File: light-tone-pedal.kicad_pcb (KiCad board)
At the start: 2 copper layers, 73.2 x 97.5 mm, 56 parts, among them U1 LM358AP, U2 LM358AP, U3 LM358AP

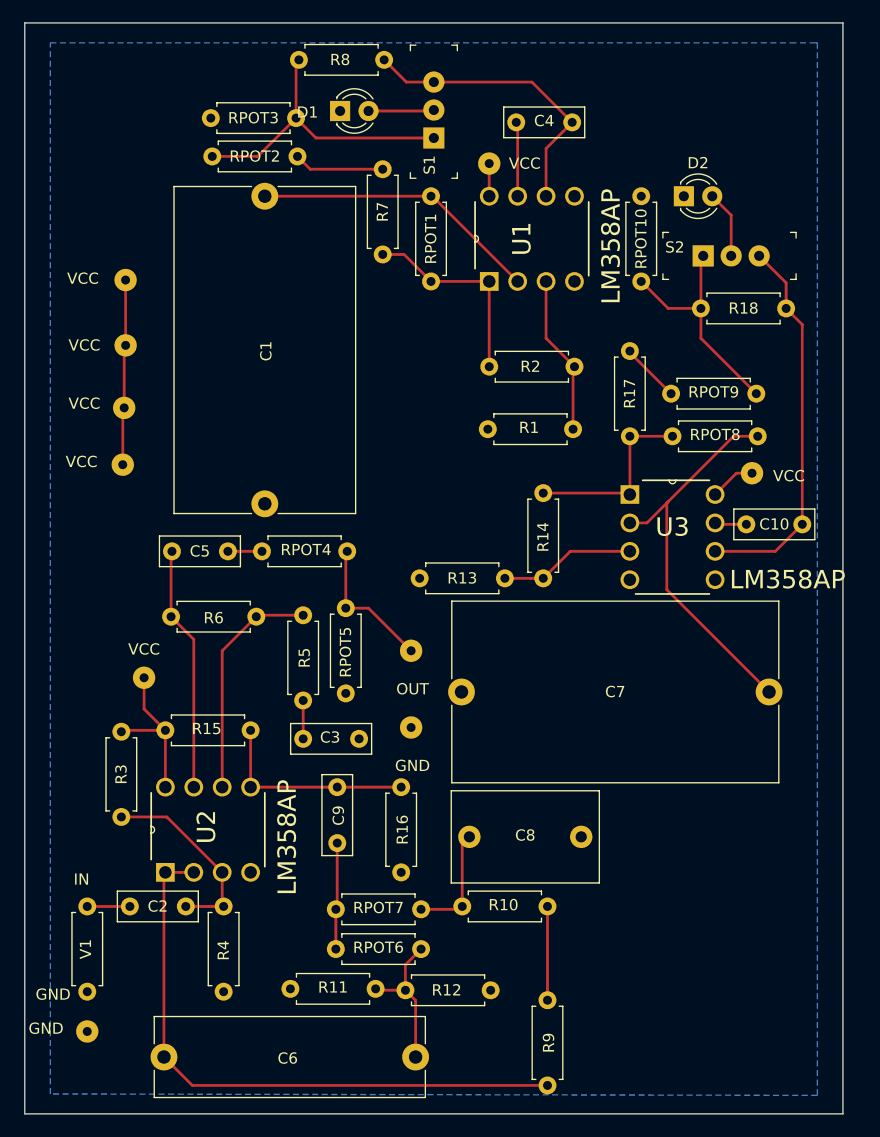
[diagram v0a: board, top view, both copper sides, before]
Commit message: Updated pdf of circuit schematic. Made pcb for light affected tone pedal.
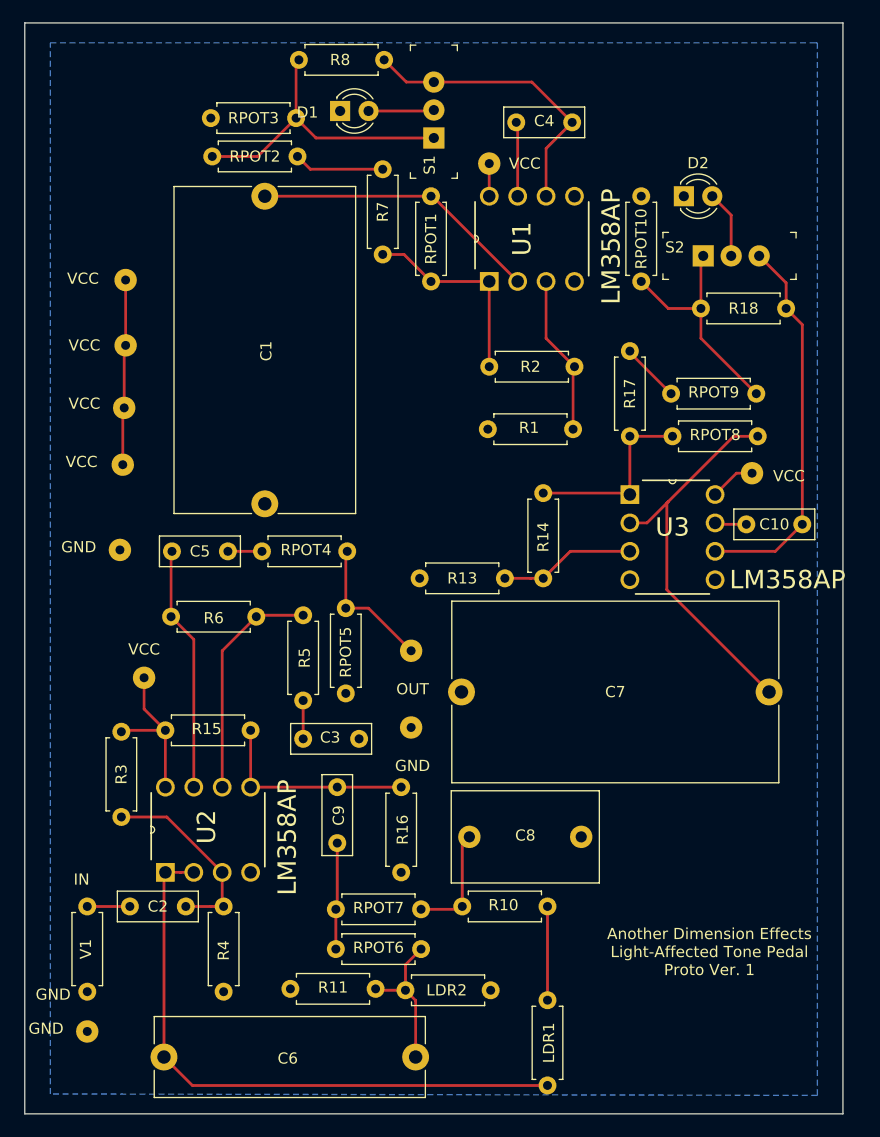
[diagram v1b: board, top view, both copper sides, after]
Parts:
- added GND: SolderWirePad_1x01_Drill0.8mm, Connector_Wire:SolderWirePad_1x01_Drill0.8mm, F.Cu at (102.7, 83.4)
- LDR1: renamed from R9; value 3k -> RLDR3k-11k
- LDR2: renamed from R12; value 3k -> RLDR3k-11k
- RPOT1, RPOT8: value R -> R20kLin
- RPOT10, RPOT2, RPOT3, RPOT9: value R -> R10kLin
- RPOT4, RPOT5: value R -> R1MegLog
- RPOT6, RPOT7: value R -> R100kLin
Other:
- board text added: "Another Dimension Effects Light-Affected Tone Pedal Proto Ver. 1"

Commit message: Added a low pass filter to power of circuit to take out noise from power supply.
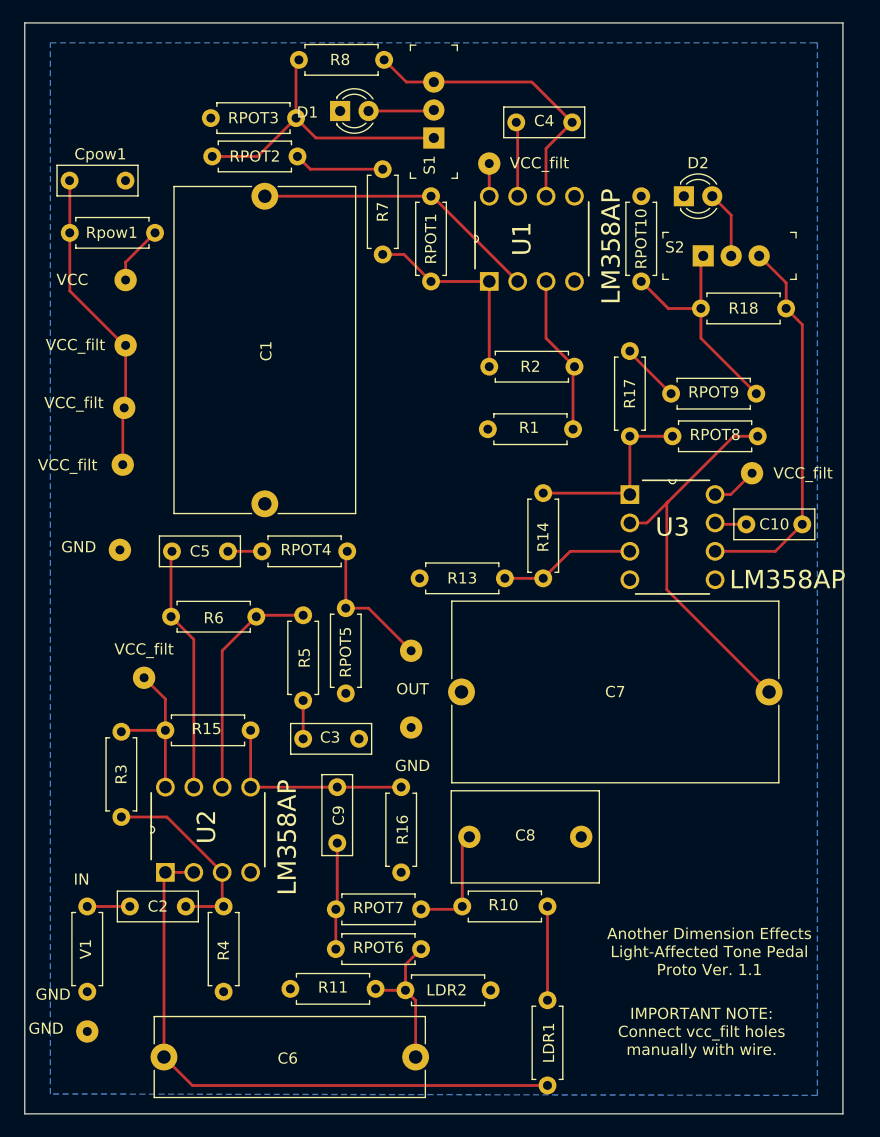
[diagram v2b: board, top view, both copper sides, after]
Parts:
- removed the VCC at (103.0, 75.8)
- removed the VCC at (103.1, 70.7)
- removed the VCC at (103.3, 65.2)
- added Cpow1: 100u, Capacitor_THT:C_Disc_D7.0mm_W2.5mm_P5.00mm, F.Cu at (98.2, 50.4)
- added Rpow1: 200, Resistor_THT:R_Axial_DIN0207_L6.3mm_D2.5mm_P7.62mm_Horizontal, F.Cu at (98.3, 55.1)
- added VCC_filt: SolderWirePad_1x01_Drill0.8mm, Connector_Wire:SolderWirePad_1x01_Drill0.8mm, F.Cu at (103.0, 75.8)
- added VCC_filt: SolderWirePad_1x01_Drill0.8mm, Connector_Wire:SolderWirePad_1x01_Drill0.8mm, F.Cu at (103.1, 70.7)
- added VCC_filt: SolderWirePad_1x01_Drill0.8mm, Connector_Wire:SolderWirePad_1x01_Drill0.8mm, F.Cu at (103.3, 65.2)
- renumbered VCC to VCC_filt
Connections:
- R15 pad 1: VCC -> vcc_filtered
- R3 pad 1: VCC -> vcc_filtered
- U1 pad 8: VCC -> vcc_filtered
- U2 pad 8: VCC -> vcc_filtered
- U3 pad 8: VCC -> vcc_filtered
- VCC_filt pad 1: VCC -> vcc_filtered (x3)
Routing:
- net vcc_filtered: track 0.00 -> 49.4 mm
- net VCC: track 38.2 -> 5.31 mm
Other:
- board text added: "Another Dimension Effects Light-Affected Tone Pedal Proto Ver. 1.1"
- board text added: "IMPORTANT NOTE: Connect vcc_filt holes manually with wire."
- board text removed: "Another Dimension Effects Light-Affected Tone Pedal Proto Ver. 1"

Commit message: Added polarity symbols on pcb for capacitors for the case of when polarized capacitors are used.
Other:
- board text added: "+"
- board text added: "-"
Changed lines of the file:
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@@
   (general
     (thickness 1.6)
-    (drawings 8)
+    (drawings 30)
     (tracks 127)
     (zones 0)
@@
     (visible_elements FFFFFF7F)
     (pcbplotparams
-      (layerselection 0x3d0fc_ffffffff)
+      (layerselection 0x3d0ff_ffffffff)
       (usegerberextensions false)
       (usegerberattributes false)
@@
     )
   )
+  (gr_text + (at 119.08028 102.44582) (layer F.SilkS)
+    (effects (font (size 1 1) (thickness 0.15)))
+  )
+  (gr_text - (at 124.079 102.53726) (layer F.SilkS)
+    (effects (font (size 1 1) (thickness 0.15)))
+  )
+  (gr_text - (at 112.52708 85.93074) (layer F.SilkS)
+    (effects (font (size 1 1) (thickness 0.15)))
+  )
+  (gr_text + (at 107.25912 85.88502) (layer F.SilkS)
+    (effects (font (size 1 1) (thickness 0.15)))
+  )
+  (gr_text - (at 108.68152 117.51056) (layer F.SilkS)
+    (effects (font (size 1 1) (thickness 0.15)))
+  )
+  (gr_text + (at 103.36784 117.57406) (layer F.SilkS)
+    (effects (font (size 1 1) (thickness 0.15)))
+  )
+  (gr_text + (at 97.45472 48.22952) (layer F.SilkS)
+    (effects (font (size 1 1) (thickness 0.15)))
+  )
+  (gr_text - (at 104.21366 48.42256) (layer F.SilkS)
+    (effects (font (size 1 1) (thickness 0.15)))
+  )
+  (gr_text + (at 109.31398 128.78054) (layer F.SilkS)
+    (effects (font (size 1 1) (thickness 0.15)))
+  )
+  (gr_text - (at 126.52502 128.53416) (layer F.SilkS)
+    (effects (font (size 1 1) (thickness 0.15)))
+  )
+  (gr_text - (at 143.90116 106.3625) (layer F.SilkS)
+    (effects (font (size 1 1) (thickness 0.15)))
+  )
+  (gr_text + (at 133.94182 106.20756) (layer F.SilkS)
+    (effects (font (size 1 1) (thickness 0.15)))
+  )
+  (gr_text + (at 157.90672 95.9739) (layer F.SilkS)
+    (effects (font (size 1 1) (thickness 0.15)))
+  )
+  (gr_text - (at 136.68502 95.9739) (layer F.SilkS)
+    (effects (font (size 1 1) (thickness 0.15)))
+  )
+  (gr_text - (at 115.34902 76.60894) (layer F.SilkS)
+    (effects (font (size 1 1) (thickness 0.15)))
+  )
+  (gr_text + (at 115.73764 54.80812) (layer F.SilkS)
+    (effects (font (size 1 1) (thickness 0.15)))
+  )
+  (gr_text + (at 143.1671 42.98188) (layer F.SilkS)
+    (effects (font (size 1 1) (thickness 0.15)))
+  )
+  (gr_text - (at 138.03376 43.15968) (layer F.SilkS)
+    (effects (font (size 1 1) (thickness 0.15)))
+  )
+  (gr_text - (at 158.60776 83.2485) (layer F.SilkS)
+    (effects (font (size 1 1) (thickness 0.15)))
+  )
+  (gr_text + (at 163.8935 83.34248) (layer F.SilkS)
+    (effects (font (size 1 1) (thickness 0.15)))
+  )
+  (gr_text + (at 120.21312 109.83468) (layer F.SilkS)
+    (effects (font (size 1 1) (thickness 0.15)))
+  )
+  (gr_text - (at 119.94134 104.65562) (layer F.SilkS)
+    (effects (font (size 1 1) (thickness 0.15)))
+  )
   (gr_text "IMPORTANT NOTE:\nConnect vcc_filt holes \nmanually with wire." (at 154.75 126.52) (layer F.SilkS)
     (effects (font (size 1 1) (thickness 0.15)))
@@
   (segment (start 130.556 59.436) (end 135.763 59.436) (width 0.25) (layer F.Cu) (net 19))
   (segment (start 135.763 59.436) (end 135.763 67.056) (width 0.25) (layer F.Cu) (net 19))
-  (segment (start 103.124 65.278) (end 103.251 65.151) (width 0.25) (layer F.Cu) (net 32))
-  (segment (start 106.807 104.648) (end 106.807 99.568) (width 0.25) (layer F.Cu) (net 32))
-  (segment (start 102.997 99.568) (end 102.87 99.695) (width 0.25) (layer F.Cu) (net 32))
-  (segment (start 106.807 99.568) (end 102.997 99.568) (width 0.25) (layer F.Cu) (net 32))
   (segment (start 103.251 57.719) (end 105.88 55.09) (width 0.25) (layer F.Cu) (net 20))
   (segment (start 103.251 59.309) (end 103.251 57.719) (width 0.25) (layer F.Cu) (net 20))
@@
   (segment (start 157.393 57.15) (end 157.393 53.507) (width 0.25) (layer F.Cu) (net 30))
   (segment (start 140.97 123.698) (end 140.97 115.316) (width 0.25) (layer F.Cu) (net 31))
+  (segment (start 103.124 65.278) (end 103.251 65.151) (width 0.25) (layer F.Cu) (net 32))
+  (segment (start 106.807 104.648) (end 106.807 99.568) (width 0.25) (layer F.Cu) (net 32))
+  (segment (start 102.997 99.568) (end 102.87 99.695) (width 0.25) (layer F.Cu) (net 32))
+  (segment (start 106.807 99.568) (end 102.997 99.568) (width 0.25) (layer F.Cu) (net 32))
   (segment (start 98.26 50.44) (end 98.24 50.42) (width 0.25) (layer F.Cu) (net 32))
   (segment (start 98.26 55.09) (end 98.26 50.44) (width 0.25) (layer F.Cu) (net 32))

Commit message: I removed the low-pass filter since it was not working out too well in pcb design.
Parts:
- removed Cpow1: 100u, Capacitor_THT:C_Disc_D7.0mm_W2.5mm_P5.00mm
- removed Rpow1: 200, Resistor_THT:R_Axial_DIN0207_L6.3mm_D2.5mm_P7.62mm_Horizontal
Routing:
- net vcc_filtered: track 49.4 -> 32.5 mm
- net VCC: track 5.31 -> 0.00 mm
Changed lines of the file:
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@@
     (thickness 1.6)
     (drawings 30)
-    (tracks 127)
+    (tracks 120)
     (zones 0)
-    (modules 59)
+    (modules 57)
     (nets 33)
   )
@@
     (add_net vout)
   )
-  (module Resistor_THT:R_Axial_DIN0207_L6.3mm_D2.5mm_P7.62mm_Horizontal (layer F.Cu)
-    (at 98.26 55.09)
-    (descr "Resistor, Axial_DIN0207 series, Axial, Horizontal, pin pitch=7.62mm, 0.25W = 1/4W, length*diameter=6.3*2.5mm^2, http://cdn-reichelt.de/documents/datenblatt/B400/1_4W%23YAG.pdf")
-    (tags "Resistor Axial_DIN0207 series Axial Horizontal pin pitch 7.62mm 0.25W = 1/4W length 6.3mm diameter 2.5mm")
-    (fp_text reference Rpow1 (at 3.75 -0.01) (layer F.SilkS)
-      (effects (font (size 1 1) (thickness 0.15)))
-    )
-    (fp_text value 200 (at 3.81 2.37) (layer F.Fab)
-      (effects (font (size 1 1) (thickness 0.15)))
-    )
-    (fp_text user %R (at 3.81 0) (layer F.Fab)
-      (effects (font (size 1 1) (thickness 0.15)))
-    )
-    (fp_line (start 8.67 -1.5) (end -1.05 -1.5) (layer F.CrtYd) (width 0.05))
-    (fp_line (start 8.67 1.5) (end 8.67 -1.5) (layer F.CrtYd) (width 0.05))
-    (fp_line (start -1.05 1.5) (end 8.67 1.5) (layer F.CrtYd) (width 0.05))
-    (fp_line (start -1.05 -1.5) (end -1.05 1.5) (layer F.CrtYd) (width 0.05))
-    (fp_line (start 7.08 1.37) (end 7.08 1.04) (layer F.SilkS) (width 0.12))
-    (fp_line (start 0.54 1.37) (end 7.08 1.37) (layer F.SilkS) (width 0.12))
-    (fp_line (start 0.54 1.04) (end 0.54 1.37) (layer F.SilkS) (width 0.12))
-    (fp_line (start 7.08 -1.37) (end 7.08 -1.04) (layer F.SilkS) (width 0.12))
-    (fp_line (start 0.54 -1.37) (end 7.08 -1.37) (layer F.SilkS) (width 0.12))
-    (fp_line (start 0.54 -1.04) (end 0.54 -1.37) (layer F.SilkS) (width 0.12))
-    (fp_line (start 7.62 0) (end 6.96 0) (layer F.Fab) (width 0.1))
-    (fp_line (start 0 0) (end 0.66 0) (layer F.Fab) (width 0.1))
-    (fp_line (start 6.96 -1.25) (end 0.66 -1.25) (layer F.Fab) (width 0.1))
-    (fp_line (start 6.96 1.25) (end 6.96 -1.25) (layer F.Fab) (width 0.1))
-    (fp_line (start 0.66 1.25) (end 6.96 1.25) (layer F.Fab) (width 0.1))
-    (fp_line (start 0.66 -1.25) (end 0.66 1.25) (layer F.Fab) (width 0.1))
-    (pad 2 thru_hole oval (at 7.62 0) (size 1.6 1.6) (drill 0.8) (layers *.Cu *.Mask)
-      (net 20 VCC))
-    (pad 1 thru_hole circle (at 0 0) (size 1.6 1.6) (drill 0.8) (layers *.Cu *.Mask)
-      (net 32 vcc_filtered))
-    (model ${KISYS3DMOD}/Resistor_THT.3dshapes/R_Axial_DIN0207_L6.3mm_D2.5mm_P7.62mm_Horizontal.wrl
-      (at (xyz 0 0 0))
-      (scale (xyz 1 1 1))
-      (rotate (xyz 0 0 0))
-    )
-  )
-  (module Capacitor_THT:C_Disc_D7.0mm_W2.5mm_P5.00mm (layer F.Cu)
-    (at 98.24 50.42)
-    (descr "C, Disc series, Radial, pin pitch=5.00mm, , diameter*width=7*2.5mm^2, Capacitor, http://cdn-reichelt.de/documents/datenblatt/B300/DS_KERKO_TC.pdf")
-    (tags "C Disc series Radial pin pitch 5.00mm  diameter 7mm width 2.5mm Capacitor")
-    (fp_text reference Cpow1 (at 2.76 -2.36) (layer F.SilkS)
-      (effects (font (size 1 1) (thickness 0.15)))
-    )
-    (fp_text value 100u (at 2.5 2.5) (layer F.Fab)
-      (effects (font (size 1 1) (thickness 0.15)))
-    )
-    (fp_text user %R (at 2.5 0) (layer F.Fab)
-      (effects (font (size 1 1) (thickness 0.15)))
-    )
-    (fp_line (start 6.25 -1.5) (end -1.25 -1.5) (layer F.CrtYd) (width 0.05))
-    (fp_line (start 6.25 1.5) (end 6.25 -1.5) (layer F.CrtYd) (width 0.05))
-    (fp_line (start -1.25 1.5) (end 6.25 1.5) (layer F.CrtYd) (width 0.05))
-    (fp_line (start -1.25 -1.5) (end -1.25 1.5) (layer F.CrtYd) (width 0.05))
-    (fp_line (start 6.12 -1.37) (end 6.12 1.37) (layer F.SilkS) (width 0.12))
-    (fp_line (start -1.12 -1.37) (end -1.12 1.37) (layer F.SilkS) (width 0.12))
-    (fp_line (start -1.12 1.37) (end 6.12 1.37) (layer F.SilkS) (width 0.12))
-    (fp_line (start -1.12 -1.37) (end 6.12 -1.37) (layer F.SilkS) (width 0.12))
-    (fp_line (start 6 -1.25) (end -1 -1.25) (layer F.Fab) (width 0.1))
-    (fp_line (start 6 1.25) (end 6 -1.25) (layer F.Fab) (width 0.1))
-    (fp_line (start -1 1.25) (end 6 1.25) (layer F.Fab) (width 0.1))
-    (fp_line (start -1 -1.25) (end -1 1.25) (layer F.Fab) (width 0.1))
-    (pad 2 thru_hole circle (at 5 0) (size 1.6 1.6) (drill 0.8) (layers *.Cu *.Mask)
-      (net 2 GND))
-    (pad 1 thru_hole circle (at 0 0) (size 1.6 1.6) (drill 0.8) (layers *.Cu *.Mask)
-      (net 32 vcc_filtered))
-    (model ${KISYS3DMOD}/Capacitor_THT.3dshapes/C_Disc_D7.0mm_W2.5mm_P5.00mm.wrl
-      (at (xyz 0 0 0))
-      (scale (xyz 1 1 1))
-      (rotate (xyz 0 0 0))
-    )
-  )
   (module Connector_Wire:SolderWirePad_1x01_Drill0.8mm (layer F.Cu)
     (at 102.743 83.439)
@@
   (segment (start 130.556 59.436) (end 135.763 59.436) (width 0.25) (layer F.Cu) (net 19))
   (segment (start 135.763 59.436) (end 135.763 67.056) (width 0.25) (layer F.Cu) (net 19))
-  (segment (start 103.251 57.719) (end 105.88 55.09) (width 0.25) (layer F.Cu) (net 20))
-  (segment (start 103.251 59.309) (end 103.251 57.719) (width 0.25) (layer F.Cu) (net 20))
   (segment (start 115.062 89.281) (end 114.935 89.408) (width 0.25) (layer F.Cu) (net 21))
   (segment (start 119.126 89.281) (end 115.062 89.281) (width 0.25) (layer F.Cu) (net 21))
@@
   (segment (start 102.997 99.568) (end 102.87 99.695) (width 0.25) (layer F.Cu) (net 32))
   (segment (start 106.807 99.568) (end 102.997 99.568) (width 0.25) (layer F.Cu) (net 32))
-  (segment (start 98.26 50.44) (end 98.24 50.42) (width 0.25) (layer F.Cu) (net 32))
-  (segment (start 98.26 55.09) (end 98.26 50.44) (width 0.25) (layer F.Cu) (net 32))
   (segment (start 135.763 51.816) (end 135.763 48.895) (width 0.25) (layer F.Cu) (net 32))
   (segment (start 106.807 96.774) (end 104.902 94.869) (width 0.25) (layer F.Cu) (net 32))
@@
   (segment (start 157.353 78.486) (end 159.258 76.581) (width 0.25) (layer F.Cu) (net 32))
   (segment (start 155.956 78.486) (end 157.353 78.486) (width 0.25) (layer F.Cu) (net 32))
-  (segment (start 103.251 65.151) (end 103.131 65.151) (width 0.25) (layer F.Cu) (net 32))
-  (segment (start 98.26 60.28) (end 98.26 55.09) (width 0.25) (layer F.Cu) (net 32))
-  (segment (start 103.131 65.151) (end 98.26 60.28) (width 0.25) (layer F.Cu) (net 32))
   (segment (start 103.251 70.612) (end 103.124 70.739) (width 0.25) (layer F.Cu) (net 32))
   (segment (start 103.251 65.151) (end 103.251 70.612) (width 0.25) (layer F.Cu) (net 32))
